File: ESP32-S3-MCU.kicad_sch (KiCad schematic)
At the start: 24 parts, among them U1 ESP32-S3, Y1 Crystal_GND24_Small

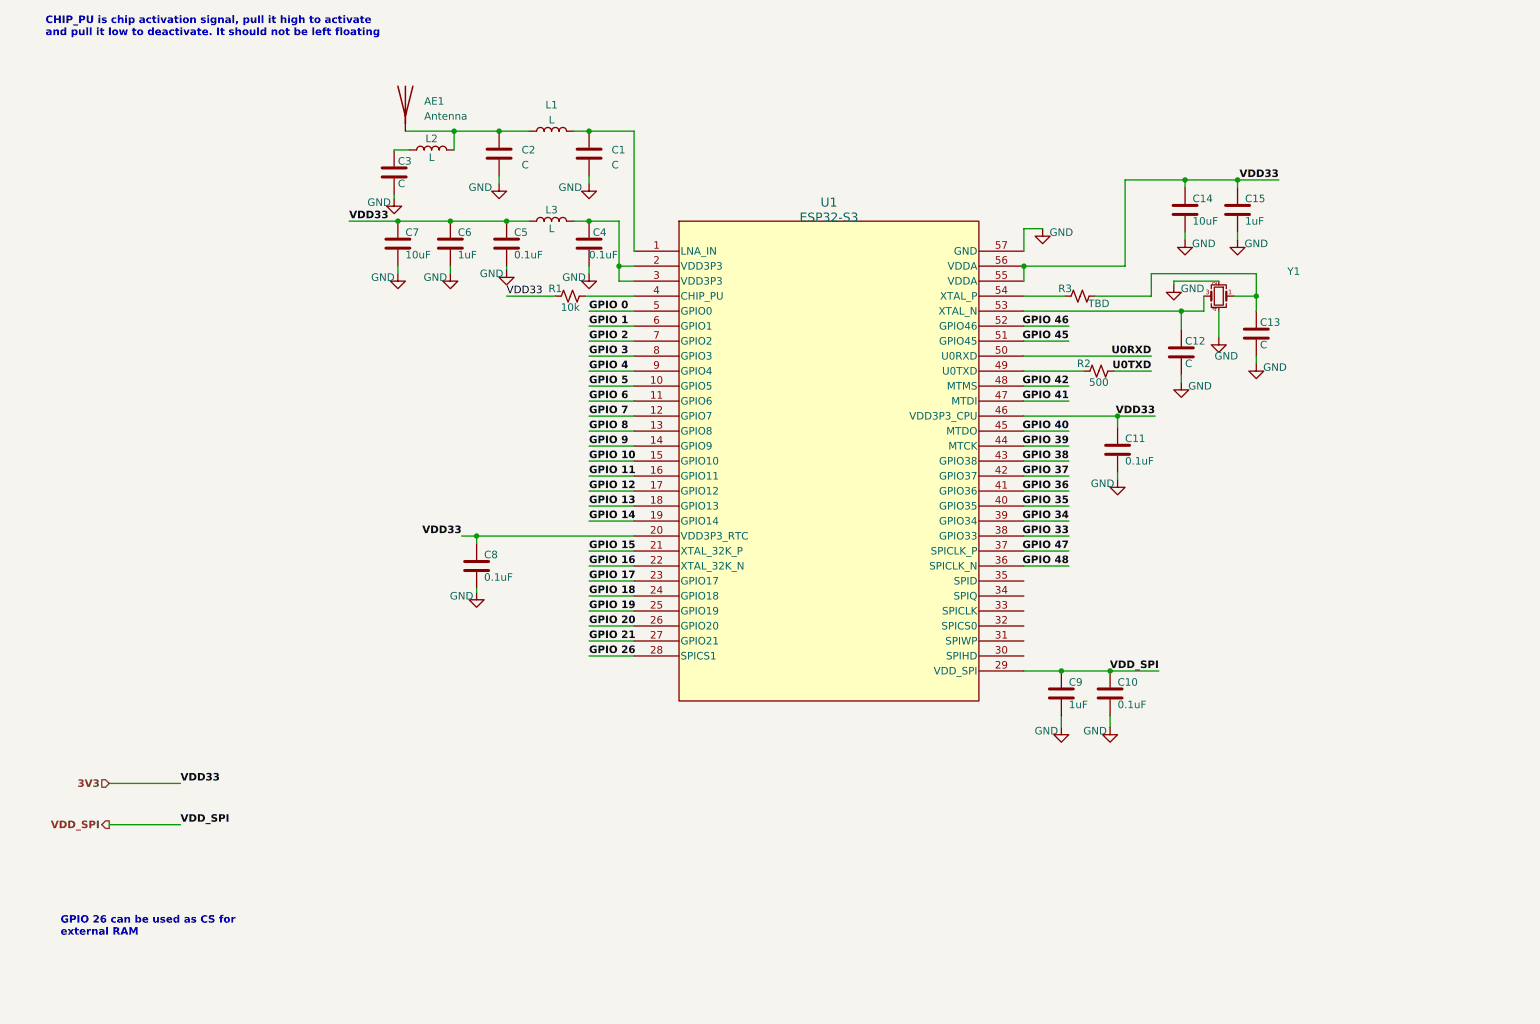
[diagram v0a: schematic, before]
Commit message: Added USB-To-UART Converter
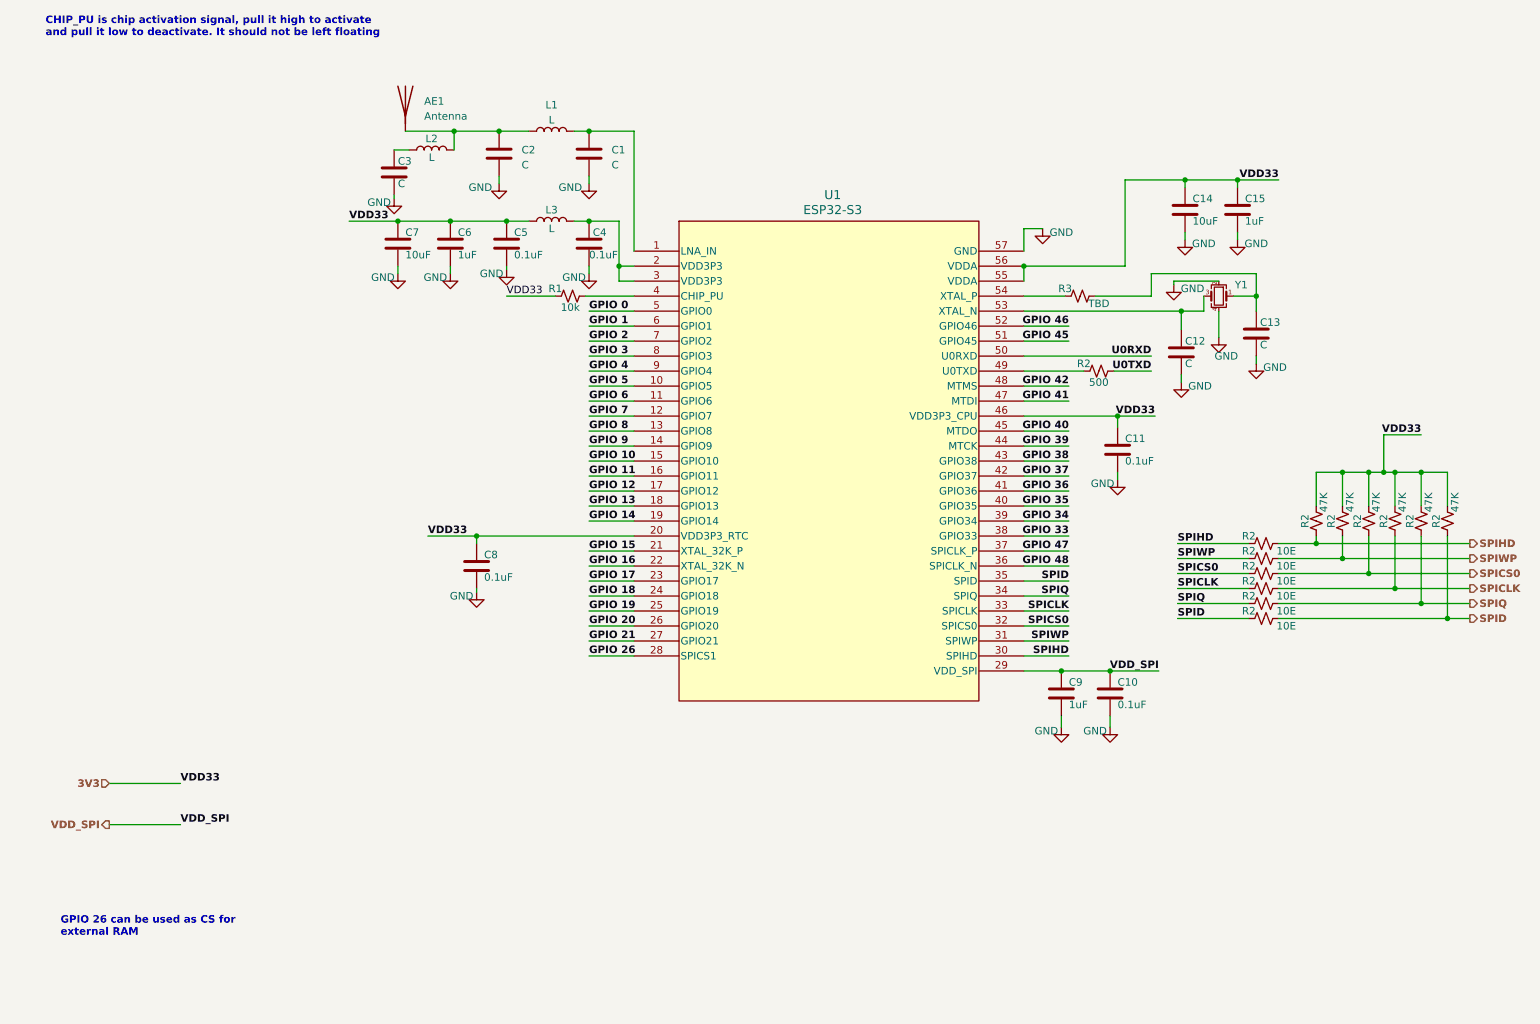
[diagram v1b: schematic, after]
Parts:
- added R2 (x6): 10E, symbol ESP32-S3_DB:R_Small_US
- added R2 (x6): 47K, symbol ESP32-S3_DB:R_Small_US
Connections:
- net 3V3: now also R2.2, R2.2, R2.2, R2.2, R2.2, R2.2
- net SPIHD: now reaches U1.30 (SPIHD)
- net SPIHD: now also R2.1, R2.1, R2.2
- net SPIWP: now reaches U1.31 (SPIWP)
- net SPIWP: now also R2.1, R2.1, R2.2
- net SPICS0: now reaches U1.32 (SPICS0)
- net SPICS0: now also R2.1, R2.1, R2.2
- net SPICLK: now reaches U1.33 (SPICLK)
- net SPICLK: now also R2.1, R2.1, R2.2
- net SPIQ: now reaches U1.34 (SPIQ)
- net SPIQ: now also R2.1, R2.1, R2.2
- net SPID: now reaches U1.35 (SPID)
- net SPID: now also R2.1, R2.1, R2.2

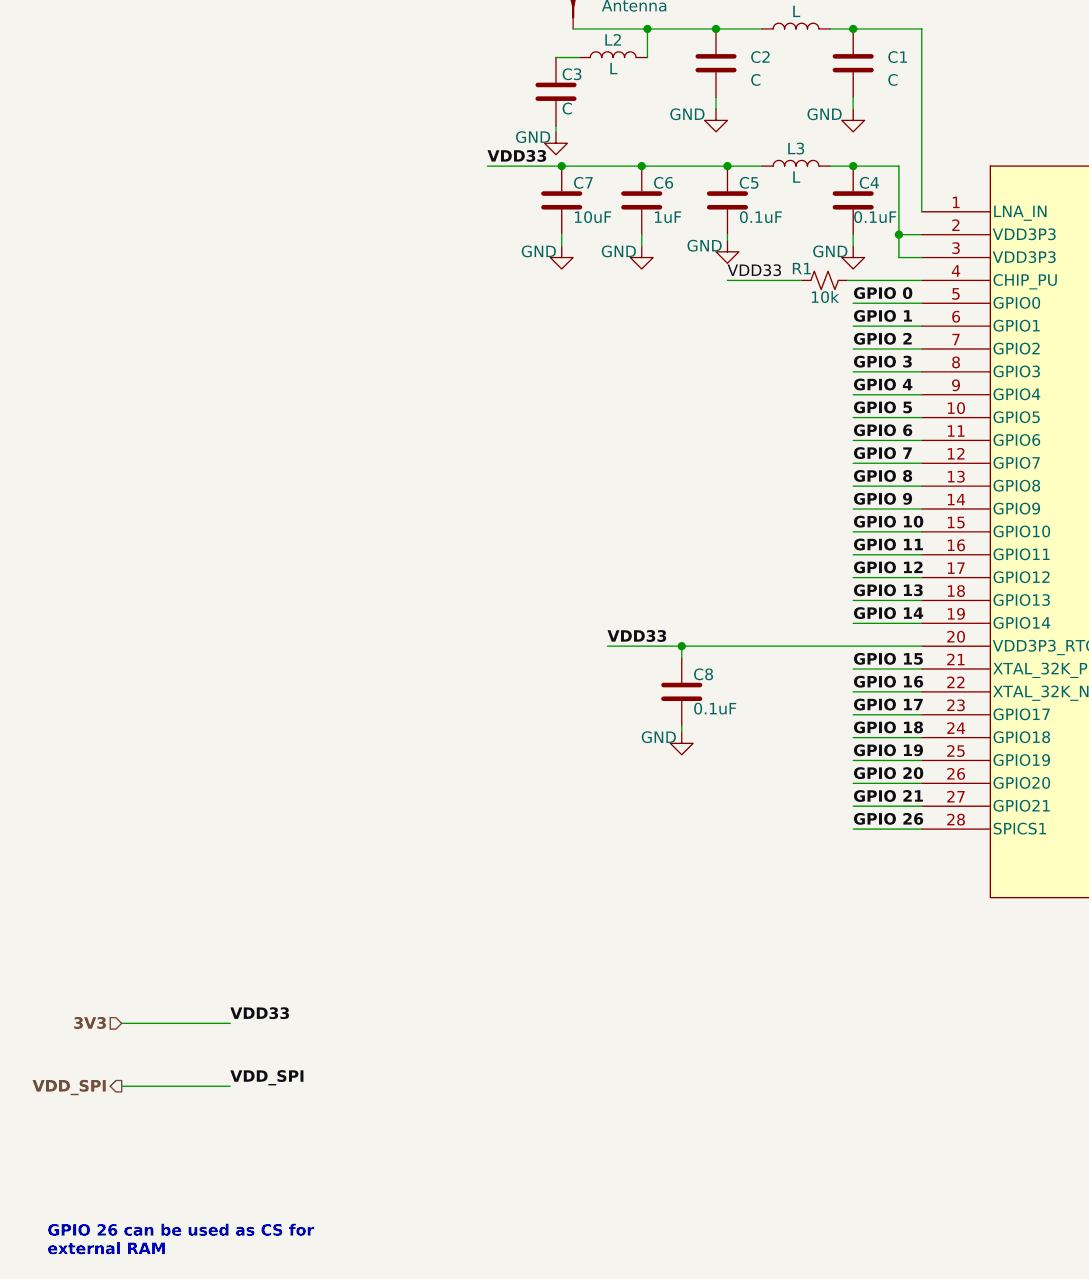
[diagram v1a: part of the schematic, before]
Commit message: Made USB-To-UART connections
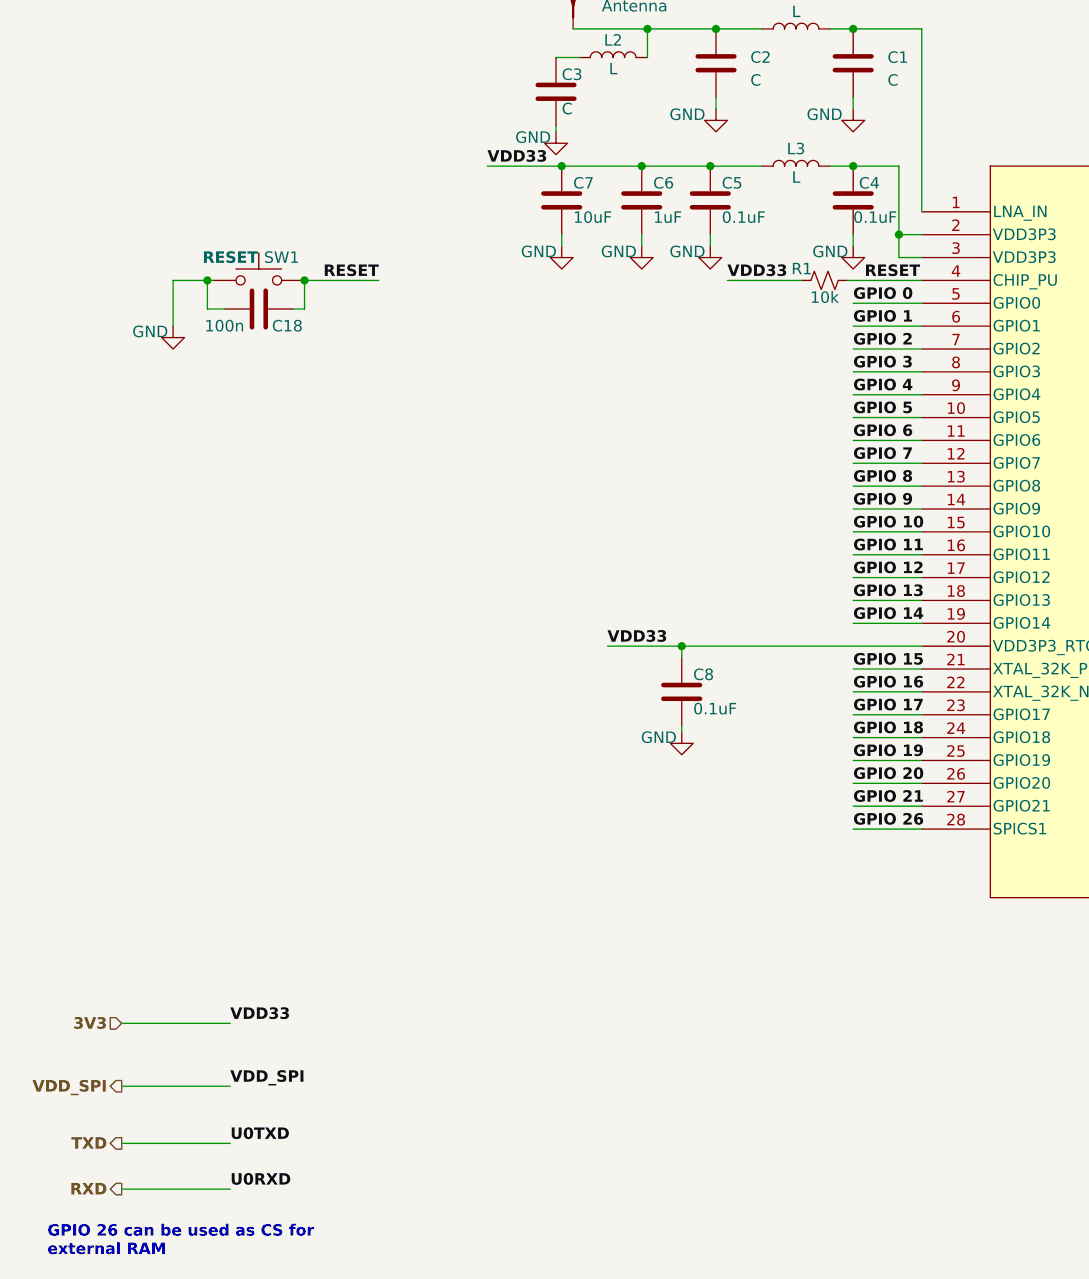
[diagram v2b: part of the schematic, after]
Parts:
- added C18: 100n, symbol ESP32-S3_DB:C
- added SW1: RESET, symbol ESP32-S3_DB:SW_Push
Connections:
- net GND: now also C18.1, SW1.1
- net RESET: now reaches R1.2, U1.4 (CHIP_PU)
- net RESET: now also C18.2, SW1.2
- net U0RXD renamed RXD
- net U0TXD renamed TXD
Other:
- moved on the sheet: C5

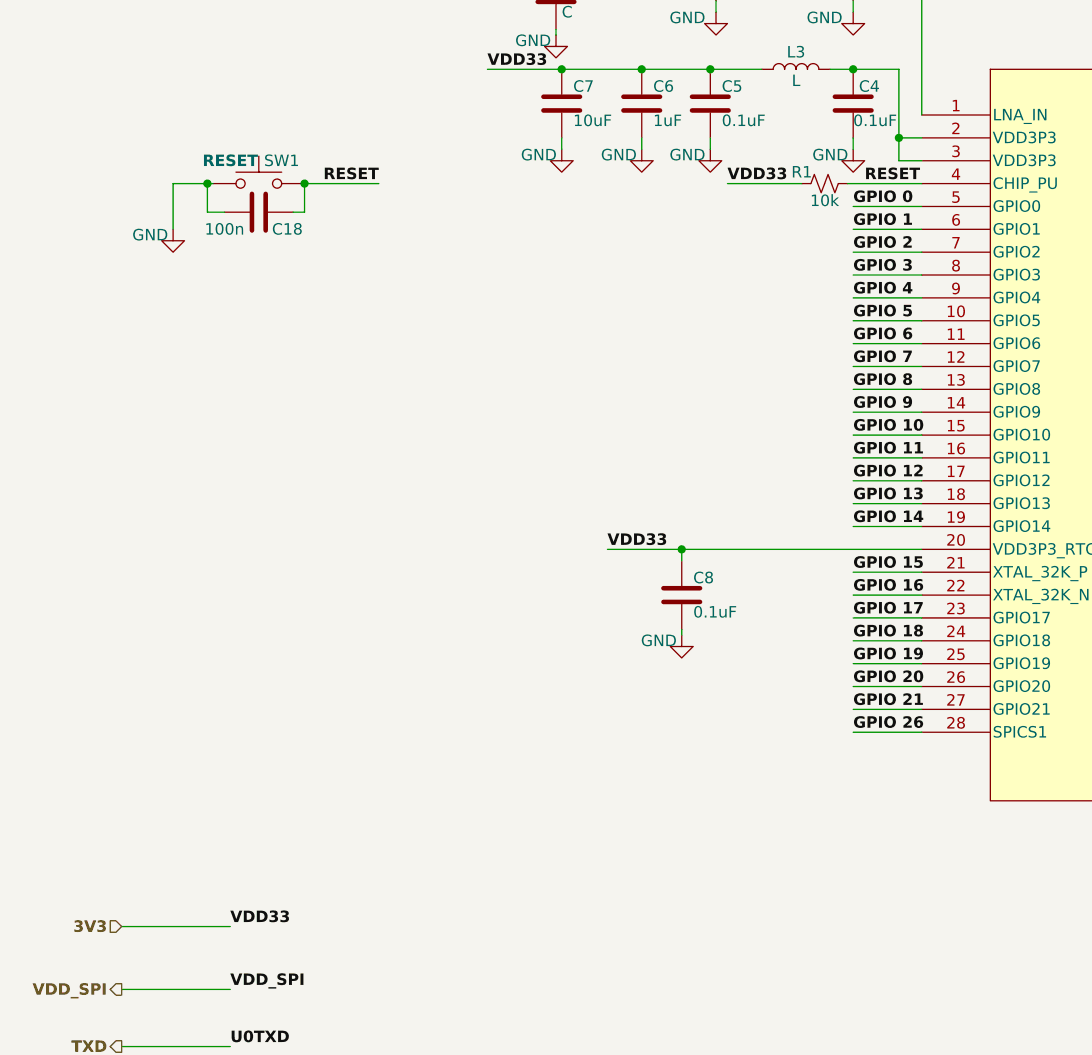
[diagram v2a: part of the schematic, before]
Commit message: Added RS-485 Transceiver
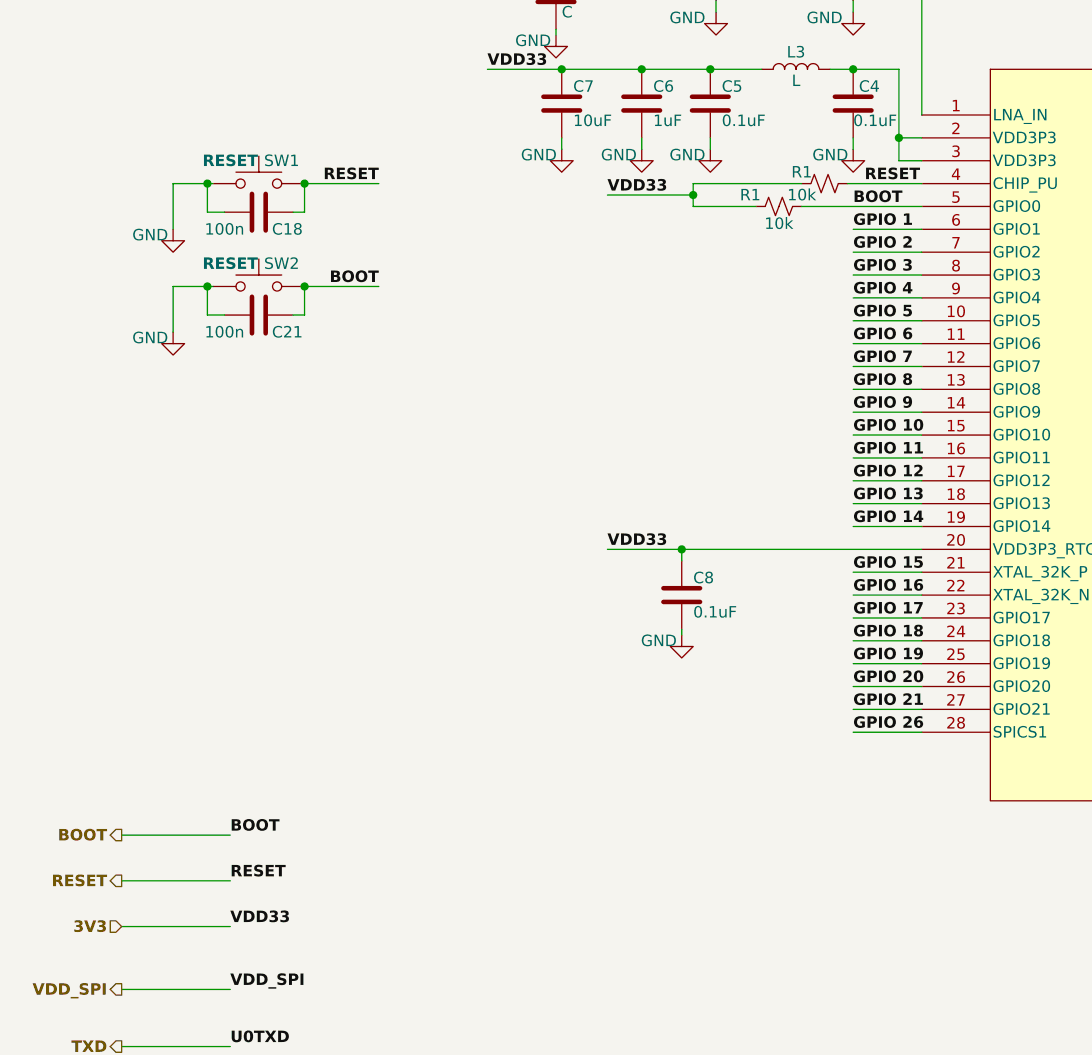
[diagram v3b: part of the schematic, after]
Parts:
- added C21: 100n, symbol ESP32-S3_DB:C
- added R1: 10k, symbol ESP32-S3_DB:R_Small_US
- added SW2: RESET, symbol ESP32-S3_DB:SW_Push
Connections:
- net 3V3: now also R1.1
- net GND: now also C21.1, SW2.1
- net GPIO 0 renamed BOOT
- net BOOT: now also C21.2, R1.2, SW2.2

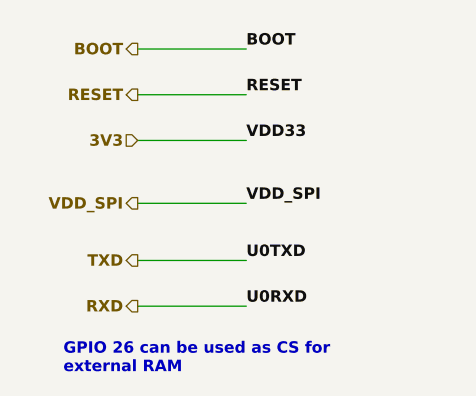
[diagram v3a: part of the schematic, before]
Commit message: Completed RS-485 connections
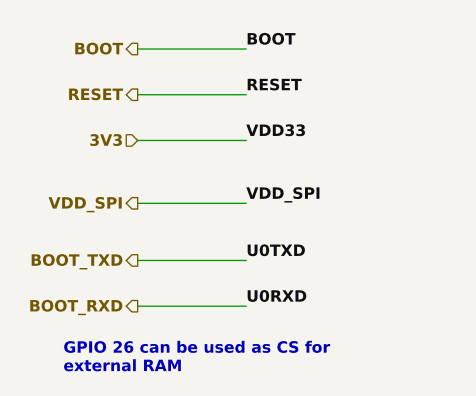
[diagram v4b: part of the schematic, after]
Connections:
- net RXD renamed BOOT_RXD
- net TXD renamed BOOT_TXD
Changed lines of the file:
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@@
     (effects (font (size 1.27 1.27) bold (color 132 0 0 1)) (justify right))
   )
-  (hierarchical_label "RXD" (shape output) (at 32.385 170.815 180) (fields_autoplaced)
+  (hierarchical_label "BOOT_RXD" (shape output) (at 32.385 170.815 180) (fields_autoplaced)
     (effects (font (size 1.27 1.27) bold (color 0 0 255 1)) (justify right))
   )
-  (hierarchical_label "TXD" (shape output) (at 32.385 165.735 180) (fields_autoplaced)
+  (hierarchical_label "BOOT_TXD" (shape output) (at 32.385 165.735 180) (fields_autoplaced)
     (effects (font (size 1.27 1.27) bold (color 0 0 255 1)) (justify right))
   )
